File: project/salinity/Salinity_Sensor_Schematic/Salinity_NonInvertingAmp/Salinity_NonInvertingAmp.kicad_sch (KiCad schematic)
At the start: 10 parts, among them U1 MCP6L01, U2 MCP6L01

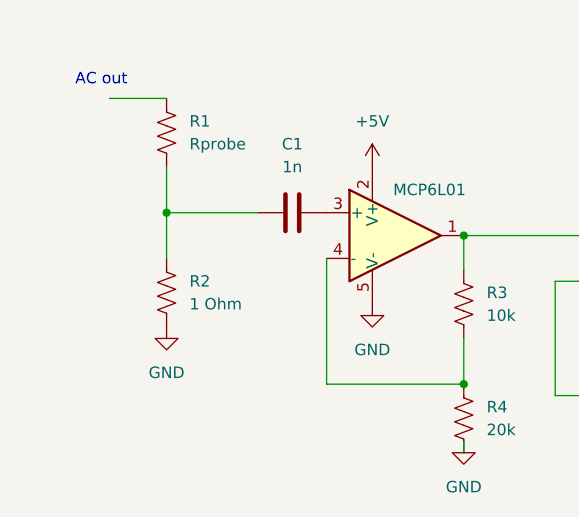
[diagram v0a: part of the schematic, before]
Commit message: Salinity Modifications
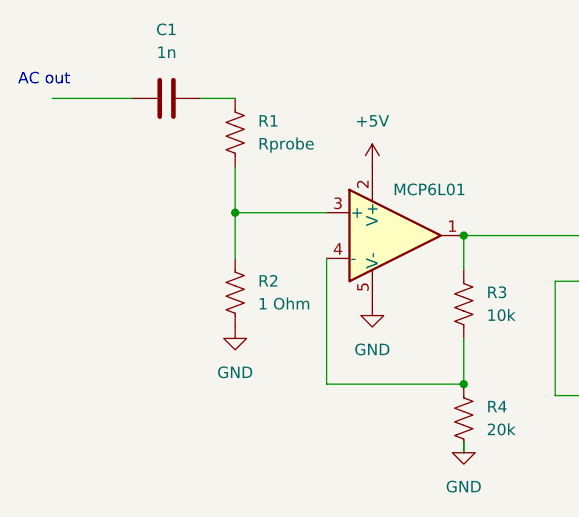
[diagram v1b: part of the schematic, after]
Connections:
- net at C1.2: now also R1.1; no longer U1.3 (+)
- net at R1.2, R2.1: now also U1.3 (+); no longer C1.1
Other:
- moved on the sheet: R1, R2
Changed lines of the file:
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@@
   (junction (at 87.63 102.87) (diameter 0) (color 0 0 0 0)
   )
-  (junction (at 54.61 83.82) (diameter 0) (color 0 0 0 0)
+  (junction (at 62.23 83.82) (diameter 0) (color 0 0 0 0)
   )
   (junction (at 123.19 88.9) (diameter 0) (color 0 0 0 0)
@@
   (junction (at 138.43 88.9) (diameter 0) (color 0 0 0 0)
   )
-  (wire (pts (xy 54.61 78.74) (xy 54.61 83.82))
+  (wire (pts (xy 41.91 71.12) (xy 50.8 71.12))
+    (stroke (width 0) (type default))
+  )
+  (wire (pts (xy 62.23 78.74) (xy 62.23 83.82))
+    (stroke (width 0) (type default))
+  )
+  (wire (pts (xy 58.42 71.12) (xy 62.23 71.12))
     (stroke (width 0) (type default))
   )
@@
     (stroke (width 0) (type default))
   )
-  (wire (pts (xy 54.61 83.82) (xy 64.77 83.82))
+  (wire (pts (xy 62.23 83.82) (xy 72.39 83.82))
     (stroke (width 0) (type default))
   )
@@
     (stroke (width 0) (type default))
   )
-  (wire (pts (xy 54.61 83.82) (xy 54.61 88.9))
+  (wire (pts (xy 62.23 83.82) (xy 62.23 88.9))
     (stroke (width 0) (type default))
   )
@@
   )
   (wire (pts (xy 138.43 88.9) (xy 147.32 88.9))
-    (stroke (width 0) (type default))
-  )
-  (wire (pts (xy 48.26 71.12) (xy 54.61 71.12))
     (stroke (width 0) (type default))
   )
@@
     (effects (font (size 1.27 1.27)) (justify left bottom))
   )
-  (text "AC out" (at 44.45 69.85 0)
+  (text "AC out" (at 38.1 69.85 0)
     (effects (font (size 1.27 1.27)) (justify left bottom))
   )
@@
     )
   )
+  (symbol (lib_id "Device:C") (at 54.61 71.12 90) (unit 1)
+    (in_bom yes) (on_board yes) (dnp no) (fields_autoplaced)
+    (property "Reference" "C1" (at 54.61 63.5 90)
+      (effects (font (size 1.27 1.27)))
+    )
+    (property "Value" "1n" (at 54.61 66.04 90)
+      (effects (font (size 1.27 1.27)))
+    )
+    (property "Footprint" "" (at 58.42 70.1548 0)
+      (effects (font (size 1.27 1.27)) hide)
+    )
+    (property "Datasheet" "~" (at 54.61 71.12 0)
+      (effects (font (size 1.27 1.27)) hide)
+    )
+    (pin "1")
+    (pin "2")
+    (instances
+      (project "Salinity_NonInvertingAmp"
+        (path "/c65a21d9-20a5-4e14-a1e3-194a093334b0"
+          (reference "C1") (unit 1)
+        )
+      )
+    )
+  )
   (symbol (lib_id "Amplifier_Operational:MCP6L01Rx-xOT") (at 107.95 88.9 0) (unit 1)
     (in_bom yes) (on_board yes) (dnp no)
@@
     )
   )
-  (symbol (lib_id "Device:R_US") (at 54.61 74.93 0) (unit 1)
-    (in_bom yes) (on_board yes) (dnp no) (fields_autoplaced)
-    (property "Reference" "R1" (at 57.15 73.66 0)
-      (effects (font (size 1.27 1.27)) (justify left))
-    )
-    (property "Value" "Rprobe" (at 57.15 76.2 0)
-      (effects (font (size 1.27 1.27)) (justify left))
-    )
-    (property "Footprint" "" (at 55.626 75.184 90)
-      (effects (font (size 1.27 1.27)) hide)
-    )
-    (property "Datasheet" "~" (at 54.61 74.93 0)
+  (symbol (lib_id "Device:R_US") (at 62.23 74.93 0) (unit 1)
+    (in_bom yes) (on_board yes) (dnp no) (fields_autoplaced)
+    (property "Reference" "R1" (at 64.77 73.66 0)
+      (effects (font (size 1.27 1.27)) (justify left))
+    )
+    (property "Value" "Rprobe" (at 64.77 76.2 0)
+      (effects (font (size 1.27 1.27)) (justify left))
+    )
+    (property "Footprint" "" (at 63.246 75.184 90)
+      (effects (font (size 1.27 1.27)) hide)
+    )
+    (property "Datasheet" "~" (at 62.23 74.93 0)
       (effects (font (size 1.27 1.27)) hide)
     )
@@
     )
   )
-  (symbol (lib_id "power:GND") (at 54.61 96.52 0) (unit 1)
-    (in_bom yes) (on_board yes) (dnp no) (fields_autoplaced)
-    (property "Reference" "#PWR01" (at 54.61 102.87 0)
-      (effects (font (size 1.27 1.27)) hide)
-    )
-    (property "Value" "GND" (at 54.61 101.6 0)
-      (effects (font (size 1.27 1.27)))
-    )
-    (property "Footprint" "" (at 54.61 96.52 0)
-      (effects (font (size 1.27 1.27)) hide)
-    )
-    (property "Datasheet" "" (at 54.61 96.52 0)
+  (symbol (lib_id "power:GND") (at 62.23 96.52 0) (unit 1)
+    (in_bom yes) (on_board yes) (dnp no) (fields_autoplaced)
+    (property "Reference" "#PWR01" (at 62.23 102.87 0)
+      (effects (font (size 1.27 1.27)) hide)
+    )
+    (property "Value" "GND" (at 62.23 101.6 0)
+      (effects (font (size 1.27 1.27)))
+    )
+    (property "Footprint" "" (at 62.23 96.52 0)
+      (effects (font (size 1.27 1.27)) hide)
+    )
+    (property "Datasheet" "" (at 62.23 96.52 0)
       (effects (font (size 1.27 1.27)) hide)
     )
@@
     )
   )
-  (symbol (lib_id "Device:C") (at 68.58 83.82 90) (unit 1)
-    (in_bom yes) (on_board yes) (dnp no) (fields_autoplaced)
-    (property "Reference" "C1" (at 68.58 76.2 90)
-      (effects (font (size 1.27 1.27)))
-    )
-    (property "Value" "1n" (at 68.58 78.74 90)
-      (effects (font (size 1.27 1.27)))
-    )
-    (property "Footprint" "" (at 72.39 82.8548 0)
-      (effects (font (size 1.27 1.27)) hide)
-    )
-    (property "Datasheet" "~" (at 68.58 83.82 0)
-      (effects (font (size 1.27 1.27)) hide)
-    )
-    (pin "2")
-    (pin "1")
-    (instances
-      (project "Salinity_NonInvertingAmp"
-        (path "/c65a21d9-20a5-4e14-a1e3-194a093334b0"
-          (reference "C1") (unit 1)
-        )
-      )
-    )
-  )
   (symbol (lib_id "power:GND") (at 105.41 96.52 0) (unit 1)
     (in_bom yes) (on_board yes) (dnp no) (fields_autoplaced)
@@
     )
   )
-  (symbol (lib_id "Device:R_US") (at 54.61 92.71 0) (unit 1)
-    (in_bom yes) (on_board yes) (dnp no) (fields_autoplaced)
-    (property "Reference" "R2" (at 57.15 91.44 0)
-      (effects (font (size 1.27 1.27)) (justify left))
-    )
-    (property "Value" "1 Ohm" (at 57.15 93.98 0)
-      (effects (font (size 1.27 1.27)) (justify left))
-    )
-    (property "Footprint" "" (at 55.626 92.964 90)
-      (effects (font (size 1.27 1.27)) hide)
-    )
-    (property "Datasheet" "~" (at 54.61 92.71 0)
-      (effects (font (size 1.27 1.27)) hide)
-    )
+  (symbol (lib_id "Device:R_US") (at 62.23 92.71 0) (unit 1)
+    (in_bom yes) (on_board yes) (dnp no) (fields_autoplaced)
+    (property "Reference" "R2" (at 64.77 91.44 0)
+      (effects (font (size 1.27 1.27)) (justify left))
+    )
+    (property "Value" "1 Ohm" (at 64.77 93.98 0)
+      (effects (font (size 1.27 1.27)) (justify left))
+    )
+    (property "Footprint" "" (at 63.246 92.964 90)
+      (effects (font (size 1.27 1.27)) hide)
+    )
+    (property "Datasheet" "~" (at 62.23 92.71 0)
+      (effects (font (size 1.27 1.27)) hide)
+    )

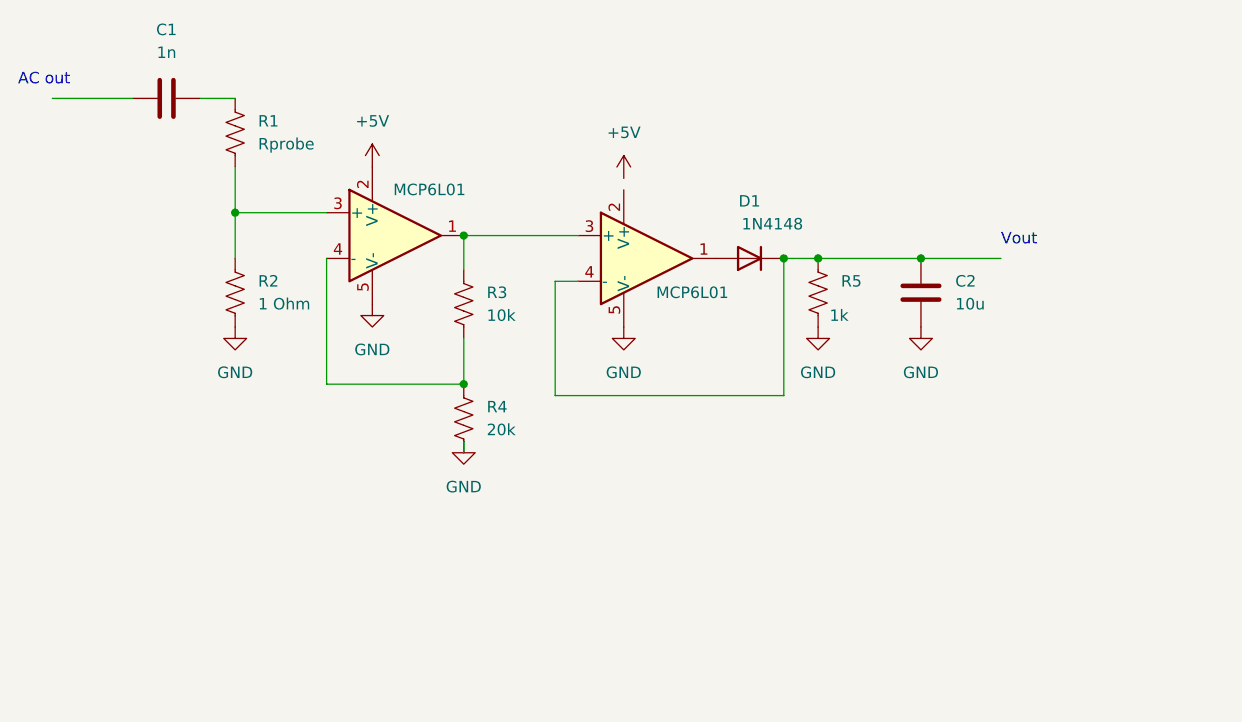
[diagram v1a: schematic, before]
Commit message: updated salinity  circuit
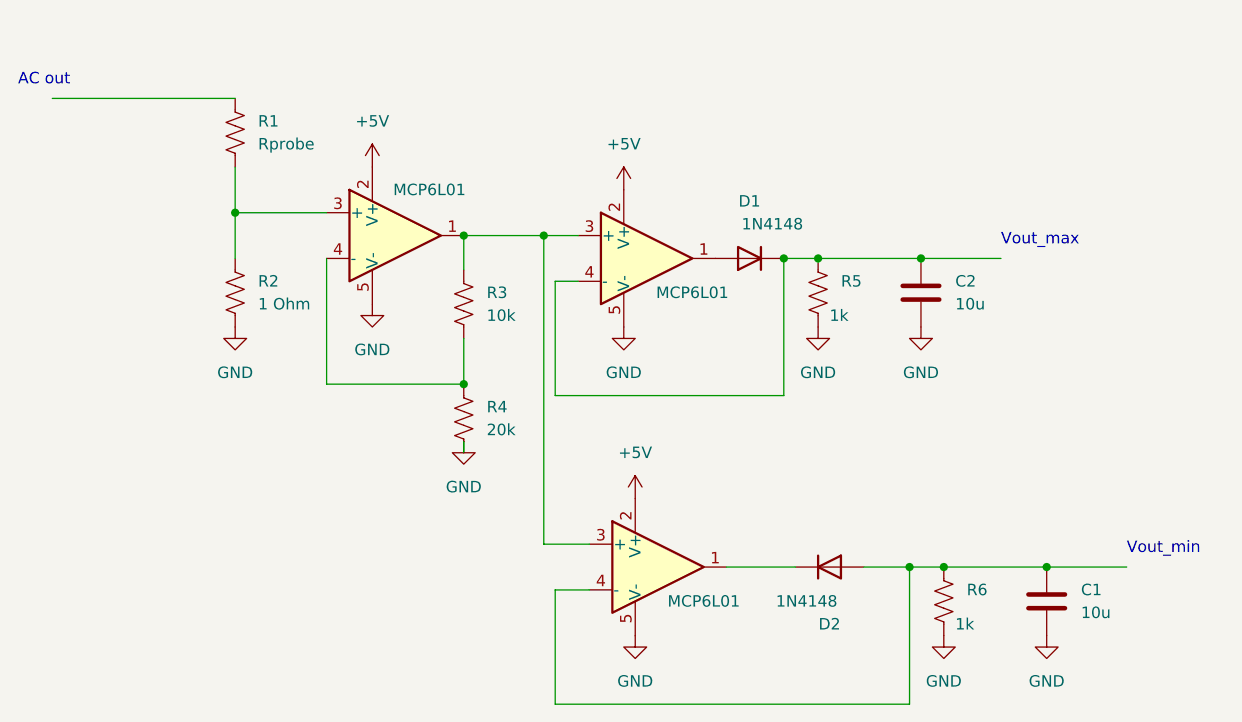
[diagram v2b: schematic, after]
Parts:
- added D2: 1N4148, symbol Device:D
- added R6: 1k, symbol Device:R_US
- added U3: MCP6L01, Package_TO_SOT_SMD:SOT-23-5, symbol Amplifier_Operational:MCP6L01Rx-xOT
- C1: value 1n -> 10u
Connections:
- net +5V: now also U2.2 (V+), U3.2 (V+)
- net GND: now also C1.2, R6.2, U3.5 (V-)
- net at R3.1, U1.1, U2.3 (+): now also U3.3 (+)
- net at C1.1: now also D2.2 (A), R6.1, U3.4 (-)
- net at R1.1: no longer C1.2
- new net: D2.1 (K), U3.1
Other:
- note added: "Vout_max"
- note added: "Vout_min"
- note removed: "Vout"
